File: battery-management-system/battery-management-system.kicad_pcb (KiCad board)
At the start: 4 copper layers, 100 x 111 mm, 212 parts, among them J1 CELL4_PLUS, J10 18V, J11 3V3, J12 AMPHENOL_micro_usb_10118194-0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, J13 I2C, J14 UART_INTERCONNECT, J15 LEDS, J16 CHARGE/DISCHARGE, J17 UART_USB, J18 rspro_header_5pin_3_5mm, J19 TEMP_CELL1, J2 CELL4_MINUS, J20 TEMP_CELL2, J21 TEMP_CELL3, J22 TEMP_CELL4, J23 Conn_01x05, J24 Charge, J25 Discharge, J3 CELL3_MINUS, J4 CELL2_MINUS, J5 CELL1_MINUS, J6 VBAT+, J7 VBAT+_CHARGE, J8 VBAT-, J9 5V, Q1 DMN3404L, Q10 DMN3404L, Q11 BS250FTA, Q12 BS250FTA, Q13 BS250FTA, Q14 BS250FTA, Q15 BS250FTA, Q16 DMN3404L, Q17 DMN3404L, Q18 DMN3404L, Q19 DMN3404L, Q2 TJ40S04M3L, Q20 DMN3404L, Q21 DMN3404L, Q22 DMN3404L, Q23 DMN3404L, Q24 DMN3404L, Q25 DMN3404L, Q26 DMN3404L, Q27 DMN3404L, Q28 DMN3404L, Q29 DMN3404L, Q3 TJ40S04M3L, Q30 DMN3404L, Q31 DMN3404L, Q32 DMN3404L, Q33 DMN3404L, Q34 DMN3404L, Q35 DMN3404L, Q36 DMN3404L, Q37 DMN3404L, Q38 DMN3404L, Q39 DMN3404L, Q4 DMN3404L, Q40 TJ40S04M3L, Q5 DMN3404L, Q6 DMN3404L, Q7 DMN3404L, Q8 DMN3404L, Q9 DMN3404L, U1 ICL7660, U10 STM32L071CZTx, U11 LM2904M8-13, U12 LM2904M8-13, U13 MC74VHC139, U2 L6982C33DR, U3 L6982C33DR, U4 ICL7660, U5 FT230XS, U6 ARM-JTAG-SWD, U7 AT24C512C, U8 NCT75DR2G, U9 STC3100

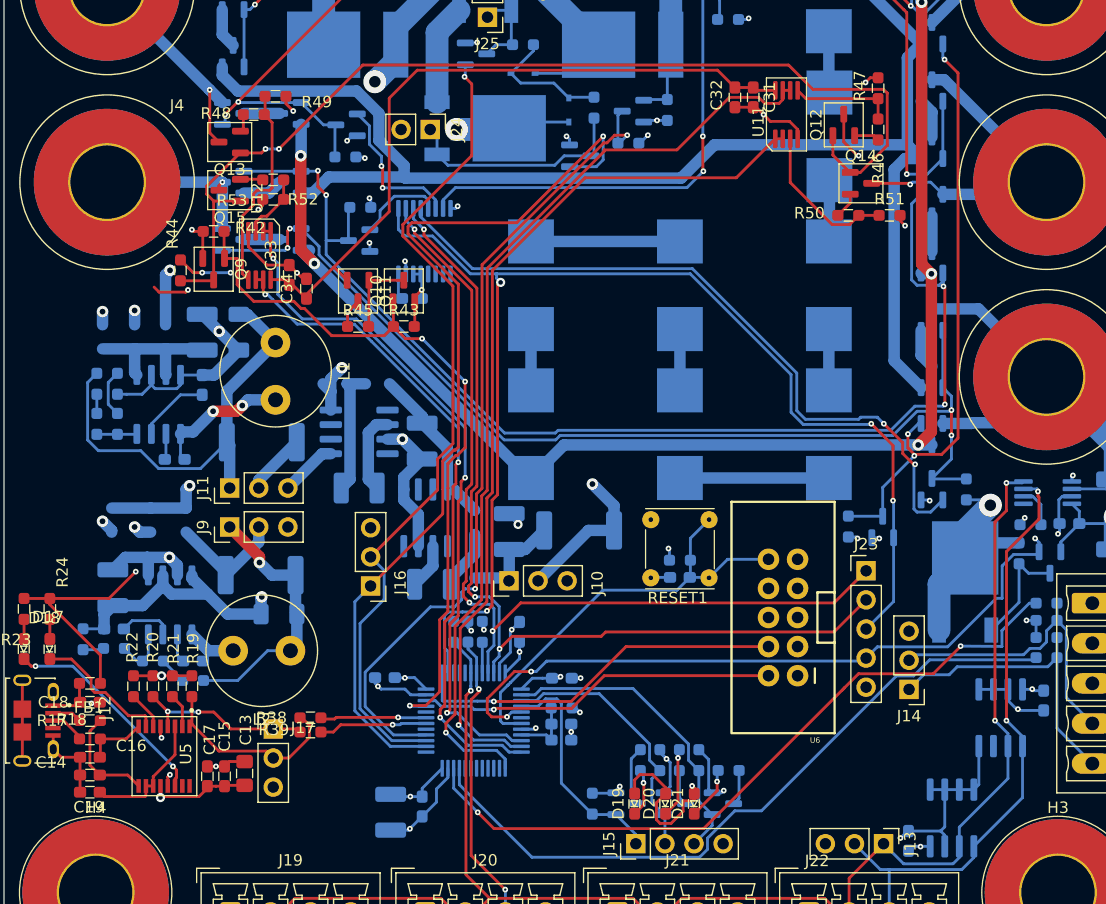
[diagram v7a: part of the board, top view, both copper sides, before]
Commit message: fix design rule errors
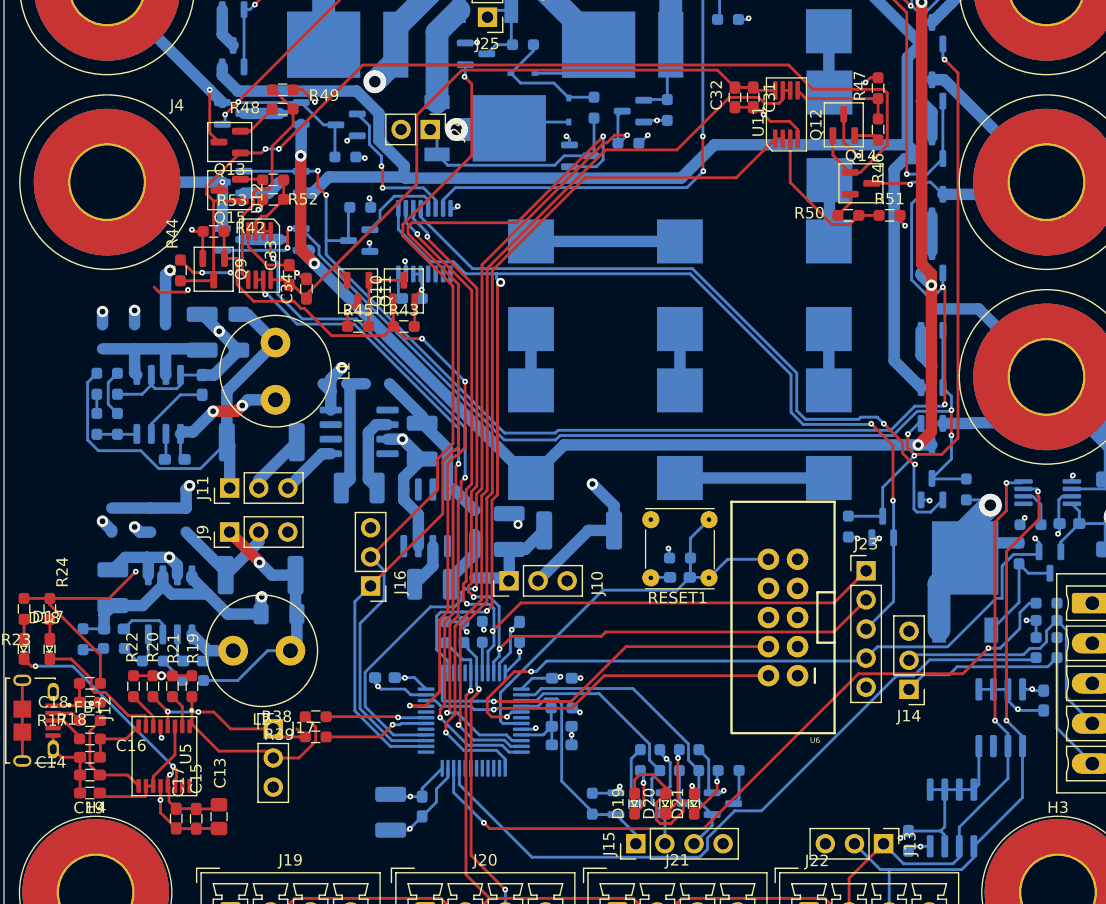
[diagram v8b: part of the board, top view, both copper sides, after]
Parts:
- moved C17 4.58 mm to (35.0, 116.5)
- moved C15 4.45 mm to (36.8, 116.6)
- moved C13 4.38 mm to (38.8, 116.4)
- moved R48 2.57 mm to (44.3, 54.6)
- moved R49 0.84 mm to (44.3, 52.9)
- moved R32 0.69 mm to (58.6, 100.3)
- moved R39 0.62 mm to (47.2, 109.4)
- moved R38 0.47 mm to (47.2, 107.7)
- moved J9 0.44 mm to (39.7, 91.5)
- moved C28 0.42 mm to (68.7, 110.1)
- moved R34 0.35 mm to (60.1, 100.3)
- moved C29 0.20 mm to (68.7, 108.5)
- moved R29 0.19 mm to (79.0, 93.8)
- moved C19 0.07 mm to (27.5, 114.3)
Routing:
- net GND: track 206.2 -> 210.0 mm, vias 43 -> 42
- net Net-(Q11-D): track 61.4 -> 59.1 mm
- net Net-(Q13-D): track 1.55 -> 3.57 mm
- net Net-(U12B-+): track 18.3 -> 20.0 mm
- net /MCU/UART_USB_TX: track 15.4 -> 16.4 mm
- net /CELL_BALANCING_STROBE: track 110.9 -> 111.9 mm
- net /18V: track 175.7 -> 176.6 mm
- net /MCU/UART_USB_RX: track 17.1 -> 17.8 mm
- net /5V_USB: track 75.0 -> 74.3 mm
- net /MCU/SCL: track 132.5 -> 133.2 mm
- net /MCU/VDDA: track 5.62 -> 6.24 mm
- net Net-(U10-PA10): track 9.29 -> 8.75 mm
- net Net-(Q24-S): track 119.7 -> 120.2 mm
